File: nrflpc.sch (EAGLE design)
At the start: 55 parts, among them IC1 LPC1111/12/13/14-HVQFN33, IC3 LM3401, IC5 LM3401, IC6 LM3401, IC7 LM3401, IC8 78L05SMD, Q2 MOSFET-PCHANNEL, Q3 MOSFET-PCHANNEL, Q4 MOSFET-PCHANNEL, Q5 MOSFET-PCHANNEL

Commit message: Basic LPC circuitry for crystal and power
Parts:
- added C1, C2: 18pF, rcl:C-EUC0402
- added C3, C4: 100nF, rcl:C-EUC0402
- added Q1: 20MHz, seb:MT-OSCILLATOR
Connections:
- new net N$19: C2.2, IC1.XTALIN, Q1.2
- new net N$29: C1.1, IC1.XTALOUT, Q1.1
- net +3V3: now also C3.1, C4.1, IC1.VDD1, IC1.VDD2
- net GND: now also C1.2, C2.1, C3.2, C4.2, IC1.VSS
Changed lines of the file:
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@@
 <part name="GND12" library="supply1" deviceset="GND" device=""/>
 <part name="IC1" library="lpc1100v1.1" deviceset="LPC1111/12/13/14-HVQFN33" device=""/>
+<part name="Q1" library="seb" deviceset="MT-OSCILLATOR" device="" value="20MHz"/>
+<part name="C1" library="rcl" deviceset="C-EU" device="C0402" value="18pF"/>
+<part name="C2" library="rcl" deviceset="C-EU" device="C0402" value="18pF"/>
+<part name="GND1" library="supply1" deviceset="GND" device=""/>
+<part name="GND2" library="supply1" deviceset="GND" device=""/>
+<part name="+3V4" library="supply1" deviceset="+3V3" device=""/>
+<part name="C3" library="rcl" deviceset="C-EU" device="C0402" value="100nF"/>
+<part name="C4" library="rcl" deviceset="C-EU" device="C0402" value="100nF"/>
+<part name="GND5" library="supply1" deviceset="GND" device=""/>
 </parts>
 <sheets>
@@
 <instance part="GND12" gate="1" x="330.2" y="93.98"/>
 <instance part="IC1" gate="G$1" x="203.2" y="142.24"/>
+<instance part="Q1" gate="G$1" x="167.64" y="142.24" rot="R90"/>
+<instance part="C1" gate="G$1" x="160.02" y="137.16" rot="R270"/>
+<instance part="C2" gate="G$1" x="157.48" y="147.32" rot="R90"/>
+<instance part="GND1" gate="1" x="149.86" y="132.08"/>
+<instance part="GND2" gate="1" x="172.72" y="91.44"/>
+<instance part="+3V4" gate="G$1" x="152.4" y="195.58"/>
+<instance part="C3" gate="G$1" x="157.48" y="180.34"/>
+<instance part="C4" gate="G$1" x="167.64" y="180.34"/>
+<instance part="GND5" gate="1" x="162.56" y="170.18"/>
 </instances>
 <busses>
@@
 <pinref part="GND12" gate="1" pin="GND"/>
 </segment>
+<segment>
+<pinref part="GND1" gate="1" pin="GND"/>
+<wire x1="149.86" y1="134.62" x2="149.86" y2="137.16" width="0.1524" layer="91"/>
+<pinref part="C2" gate="G$1" pin="1"/>
+<wire x1="154.94" y1="147.32" x2="149.86" y2="147.32" width="0.1524" layer="91"/>
+<wire x1="149.86" y1="147.32" x2="149.86" y2="137.16" width="0.1524" layer="91"/>
+<pinref part="C1" gate="G$1" pin="2"/>
+<wire x1="149.86" y1="137.16" x2="154.94" y2="137.16" width="0.1524" layer="91"/>
+<junction x="149.86" y="137.16"/>
+</segment>
+<segment>
+<pinref part="IC1" gate="G$1" pin="VSS"/>
+<pinref part="GND2" gate="1" pin="GND"/>
+<wire x1="175.26" y1="96.52" x2="172.72" y2="96.52" width="0.1524" layer="91"/>
+<wire x1="172.72" y1="96.52" x2="172.72" y2="93.98" width="0.1524" layer="91"/>
+</segment>
+<segment>
+<pinref part="C4" gate="G$1" pin="2"/>
+<wire x1="167.64" y1="175.26" x2="167.64" y2="172.72" width="0.1524" layer="91"/>
+<pinref part="C3" gate="G$1" pin="2"/>
+<wire x1="167.64" y1="172.72" x2="162.56" y2="172.72" width="0.1524" layer="91"/>
+<wire x1="162.56" y1="172.72" x2="157.48" y2="172.72" width="0.1524" layer="91"/>
+<wire x1="157.48" y1="172.72" x2="157.48" y2="175.26" width="0.1524" layer="91"/>
+<pinref part="GND5" gate="1" pin="GND"/>
+<junction x="162.56" y="172.72"/>
+</segment>
 </net>
 <net name="!RST" class="0">
@@
 <pinref part="+3V3" gate="G$1" pin="+3V3"/>
 </segment>
+<segment>
+<pinref part="IC1" gate="G$1" pin="VDD1"/>
+<pinref part="+3V4" gate="G$1" pin="+3V3"/>
+<wire x1="175.26" y1="190.5" x2="157.48" y2="190.5" width="0.1524" layer="91"/>
+<wire x1="157.48" y1="190.5" x2="152.4" y2="190.5" width="0.1524" layer="91"/>
+<wire x1="152.4" y1="190.5" x2="152.4" y2="193.04" width="0.1524" layer="91"/>
+<pinref part="IC1" gate="G$1" pin="VDD2"/>
+<wire x1="175.26" y1="185.42" x2="167.64" y2="185.42" width="0.1524" layer="91"/>
+<wire x1="167.64" y1="185.42" x2="152.4" y2="185.42" width="0.1524" layer="91"/>
+<wire x1="152.4" y1="185.42" x2="152.4" y2="190.5" width="0.1524" layer="91"/>
+<junction x="152.4" y="190.5"/>
+<pinref part="C3" gate="G$1" pin="1"/>
+<wire x1="157.48" y1="182.88" x2="157.48" y2="190.5" width="0.1524" layer="91"/>
+<junction x="157.48" y="190.5"/>
+<pinref part="C4" gate="G$1" pin="1"/>
+<wire x1="167.64" y1="182.88" x2="167.64" y2="185.42" width="0.1524" layer="91"/>
+<junction x="167.64" y="185.42"/>
+</segment>
 </net>
 <net name="CE" class="0">
@@
 </segment>
 </net>
+<net name="N$19" class="0">
+<segment>
+<pinref part="IC1" gate="G$1" pin="XTALIN"/>
+<pinref part="Q1" gate="G$1" pin="2"/>
+<wire x1="175.26" y1="144.78" x2="167.64" y2="144.78" width="0.1524" layer="91"/>
+<pinref part="C2" gate="G$1" pin="2"/>
+<wire x1="162.56" y1="147.32" x2="167.64" y2="147.32" width="0.1524" layer="91"/>
+<wire x1="167.64" y1="147.32" x2="167.64" y2="144.78" width="0.1524" layer="91"/>
+<junction x="167.64" y="144.78"/>
+</segment>
+</net>
+<net name="N$29" class="0">
+<segment>
+<pinref part="IC1" gate="G$1" pin="XTALOUT"/>
+<pinref part="Q1" gate="G$1" pin="1"/>
+<wire x1="175.26" y1="139.7" x2="167.64" y2="139.7" width="0.1524" layer="91"/>
+<pinref part="C1" gate="G$1" pin="1"/>
+<wire x1="162.56" y1="137.16" x2="167.64" y2="137.16" width="0.1524" layer="91"/>
+<wire x1="167.64" y1="137.16" x2="167.64" y2="139.7" width="0.1524" layer="91"/>
+<junction x="167.64" y="139.7"/>
+</segment>
+</net>

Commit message: Chosen good fitting PWM Pins, Reset circuitry
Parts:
- added C5: 100nF, rcl:C-EUC0402
- added R1: (no value), rcl:R-US_R0402
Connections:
- net !RST: now also C5.1, IC1.!RESET!/PIO0_0, R1.1
- net +3V3: now also R1.2
- net GND: now also C5.2
- net PB: now also IC1.SWDIO/PIO1_3/AD4/CT32B1_MAT2
- net PG: now also IC1.PIO1_6/RXD/CT32B0_MAT0
- net PR: now also IC1.PIO1_7/TXD/CT32B0_MAT1
- net PW: now also IC1.R/PIO1_2/AD3/CT32B1_MAT1
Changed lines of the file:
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@@
 <part name="C4" library="rcl" deviceset="C-EU" device="C0402" value="100nF"/>
 <part name="GND5" library="supply1" deviceset="GND" device=""/>
+<part name="R1" library="rcl" deviceset="R-US_" device="R0402"/>
+<part name="+3V5" library="supply1" deviceset="+3V3" device=""/>
+<part name="GND13" library="supply1" deviceset="GND" device=""/>
+<part name="C5" library="rcl" deviceset="C-EU" device="C0402" value="100nF"/>
 </parts>
 <sheets>
 <sheet>
 <plain>
-<wire x1="414.02" y1="213.36" x2="22.86" y2="213.36" width="0.1524" layer="94"/>
-<wire x1="22.86" y1="10.16" x2="22.86" y2="213.36" width="0.1524" layer="94"/>
+<wire x1="411.48" y1="218.44" x2="20.32" y2="218.44" width="0.1524" layer="94"/>
+<wire x1="22.86" y1="10.16" x2="20.32" y2="218.44" width="0.1524" layer="94"/>
 <wire x1="22.86" y1="10.16" x2="414.02" y2="10.16" width="0.1524" layer="94"/>
-<wire x1="414.02" y1="10.16" x2="414.02" y2="213.36" width="0.1524" layer="94"/>
+<wire x1="414.02" y1="10.16" x2="411.48" y2="218.44" width="0.1524" layer="94"/>
 <text x="106.68" y="-96.52" size="3.81" layer="94">Reichelt</text>
 <text x="81.28" y="-109.22" size="3.81" layer="94">Spule</text>
@@
 <instance part="C4" gate="G$1" x="167.64" y="180.34"/>
 <instance part="GND5" gate="1" x="162.56" y="170.18"/>
+<instance part="R1" gate="G$1" x="302.26" y="157.48" rot="R90"/>
+<instance part="+3V5" gate="G$1" x="302.26" y="167.64"/>
+<instance part="GND13" gate="1" x="302.26" y="134.62"/>
+<instance part="C5" gate="G$1" x="302.26" y="144.78"/>
 </instances>
 <busses>
@@
 <junction x="162.56" y="172.72"/>
 </segment>
+<segment>
+<pinref part="C5" gate="G$1" pin="2"/>
+<pinref part="GND13" gate="1" pin="GND"/>
+<wire x1="302.26" y1="139.7" x2="302.26" y2="137.16" width="0.1524" layer="91"/>
+</segment>
 </net>
 <net name="!RST" class="0">
@@
 <wire x1="76.2" y1="144.78" x2="73.66" y2="144.78" width="0.1524" layer="91"/>
 <label x="73.66" y="144.78" size="1.778" layer="95"/>
+</segment>
+<segment>
+<pinref part="R1" gate="G$1" pin="1"/>
+<pinref part="C5" gate="G$1" pin="1"/>
+<wire x1="302.26" y1="147.32" x2="302.26" y2="149.86" width="0.1524" layer="91"/>
+<wire x1="302.26" y1="149.86" x2="302.26" y2="152.4" width="0.1524" layer="91"/>
+<wire x1="302.26" y1="149.86" x2="289.56" y2="149.86" width="0.1524" layer="91"/>
+<junction x="302.26" y="149.86"/>
+<label x="292.1" y="149.86" size="1.778" layer="95"/>
+</segment>
+<segment>
+<pinref part="IC1" gate="G$1" pin="!RESET!/PIO0_0"/>
+<wire x1="231.14" y1="198.12" x2="241.3" y2="198.12" width="0.1524" layer="91"/>
+<label x="236.22" y="198.12" size="1.778" layer="95"/>
 </segment>
 </net>
@@
 <pinref part="IC7" gate="G$1" pin="DIM"/>
 </segment>
+<segment>
+<pinref part="IC1" gate="G$1" pin="SWDIO/PIO1_3/AD4/CT32B1_MAT2"/>
+<wire x1="231.14" y1="157.48" x2="241.3" y2="157.48" width="0.1524" layer="91"/>
+<label x="236.22" y="157.48" size="1.778" layer="95"/>
+</segment>
 </net>
 <net name="PG" class="0">
@@
 <pinref part="IC6" gate="G$1" pin="DIM"/>
 </segment>
+<segment>
+<pinref part="IC1" gate="G$1" pin="PIO1_6/RXD/CT32B0_MAT0"/>
+<wire x1="231.14" y1="149.86" x2="241.3" y2="149.86" width="0.1524" layer="91"/>
+<label x="236.22" y="149.86" size="1.778" layer="95"/>
+</segment>
 </net>
 <net name="PR" class="0">
@@
 <pinref part="IC5" gate="G$1" pin="DIM"/>
 </segment>
+<segment>
+<pinref part="IC1" gate="G$1" pin="PIO1_7/TXD/CT32B0_MAT1"/>
+<wire x1="231.14" y1="147.32" x2="241.3" y2="147.32" width="0.1524" layer="91"/>
+<label x="236.22" y="147.32" size="1.778" layer="95"/>
+</segment>
 </net>
 <net name="PW" class="0">
@@
 <label x="33.02" y="-22.86" size="1.778" layer="95"/>
 <pinref part="IC3" gate="G$1" pin="DIM"/>
+</segment>
+<segment>
+<pinref part="IC1" gate="G$1" pin="R/PIO1_2/AD3/CT32B1_MAT1"/>
+<wire x1="231.14" y1="160.02" x2="241.3" y2="160.02" width="0.1524" layer="91"/>
+<label x="236.22" y="160.02" size="1.778" layer="95"/>
 </segment>
 </net>
@@
 <junction x="167.64" y="185.42"/>
 </segment>
-</net>
+<segment>
+<pinref part="R1" gate="G$1" pin="2"/>
+<pinref part="+3V5" gate="G$1" pin="+3V3"/>
+<wire x1="302.26" y1="165.1" x2="302.26" y2="162.56" width="0.1524" layer="91"/>
+</segment>
+</net>

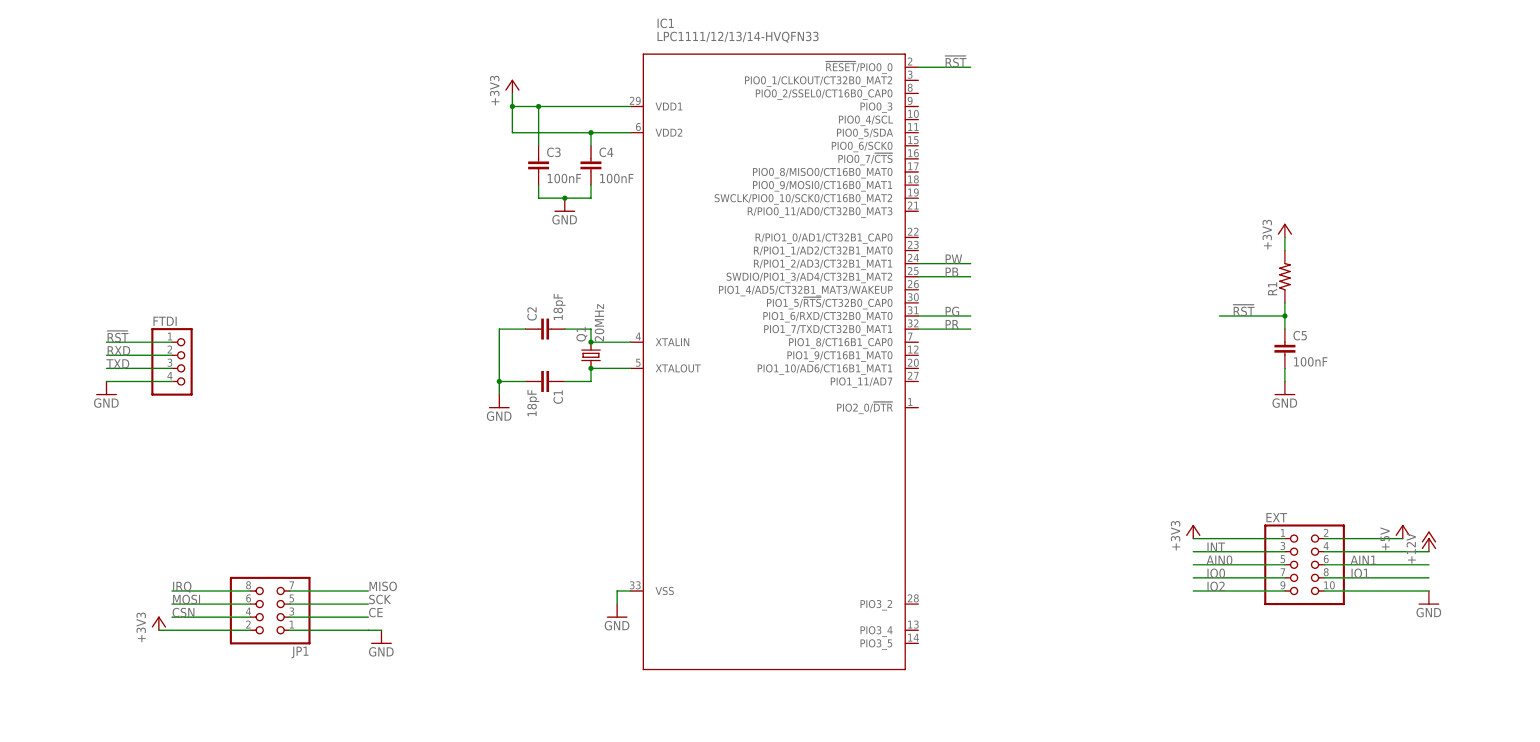
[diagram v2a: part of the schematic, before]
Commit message: Mostly final signal assignment, Starting to place
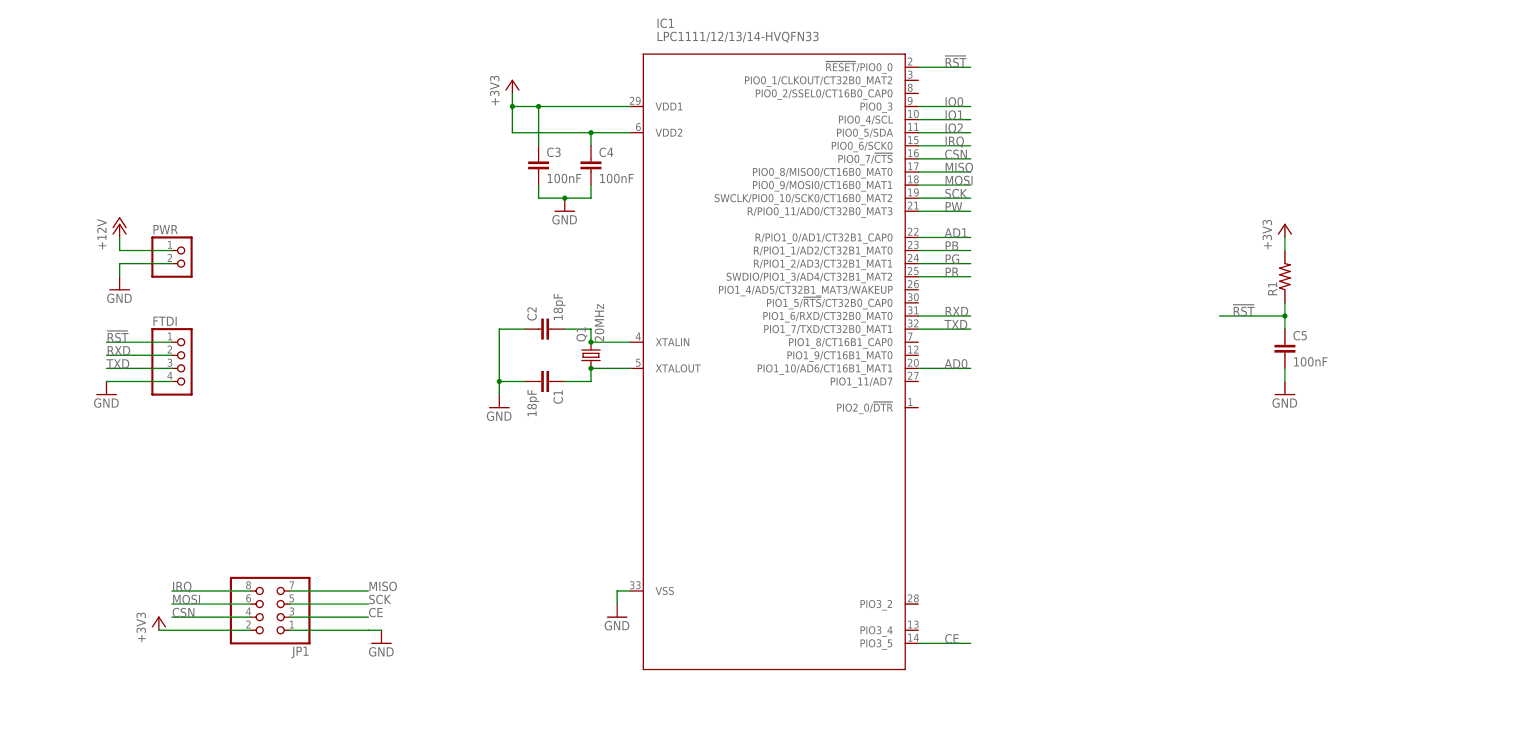
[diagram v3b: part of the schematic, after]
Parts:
- removed EXT: (no value), pinhead:PINHD-2X5
- added PWR: (no value), pinhead:PINHD-1X2
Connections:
- removed net +5V: EXT.2
- removed net AIN0: EXT.5
- removed net AIN1: EXT.6
- removed net INT: EXT.3
- new net AD0: IC1.PIO1_10/AD6/CT16B1_MAT1
- new net AD1: IC1.R/PIO1_0/AD1/CT32B1_CAP0
- net +12V: now also PWR.1; no longer EXT.4
- net +3V3: no longer EXT.1
- net CE: now also IC1.PIO3_5
- net CSN: now also IC1.PIO0_7/!CTS!
- net GND: now also PWR.2; no longer EXT.10
- net IO0: now also IC1.PIO0_3; no longer EXT.7
- net IO1: now also IC1.PIO0_4/SCL; no longer EXT.8
- net IO2: now also IC1.PIO0_5/SDA; no longer EXT.9
- net IRQ: now also IC1.PIO0_6/SCK0
- net MISO: now also IC1.PIO0_8/MISO0/CT16B0_MAT0
- net MOSI: now also IC1.PIO0_9/MOSI0/CT16B0_MAT1
- net PB: now also IC1.R/PIO1_1/AD2/CT32B1_MAT0; no longer IC1.SWDIO/PIO1_3/AD4/CT32B1_MAT2
- net PG: now also IC1.R/PIO1_2/AD3/CT32B1_MAT1; no longer IC1.PIO1_6/RXD/CT32B0_MAT0
- net PR: now also IC1.SWDIO/PIO1_3/AD4/CT32B1_MAT2; no longer IC1.PIO1_7/TXD/CT32B0_MAT1
- net PW: now also IC1.R/PIO0_11/AD0/CT32B0_MAT3; no longer IC1.R/PIO1_2/AD3/CT32B1_MAT1
- net RXD: now also IC1.PIO1_6/RXD/CT32B0_MAT0
- net SCK: now also IC1.SWCLK/PIO0_10/SCK0/CT16B0_MAT2
- net TXD: now also IC1.PIO1_7/TXD/CT32B0_MAT1
